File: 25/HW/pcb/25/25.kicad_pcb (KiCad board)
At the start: 2 copper layers, 31.5 x 31.5 mm, 5 parts

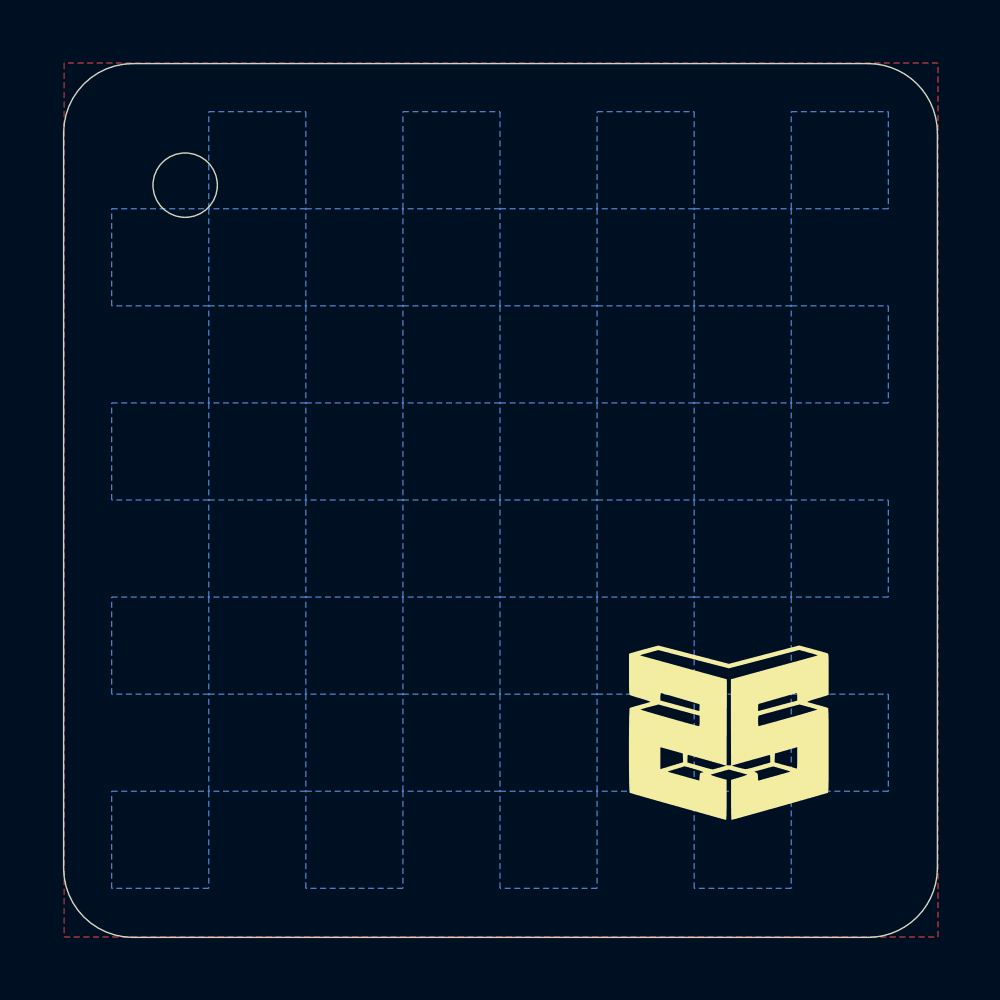
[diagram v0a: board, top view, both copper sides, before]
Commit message: Updated HW/ART and HW/PCB files for second batch of PCBs. First one had troubles with QR detection due to finder pattern with hole in it. Now only silkscreen on top, hole outside QR area (logo), and bigger drawings with metals on bottom
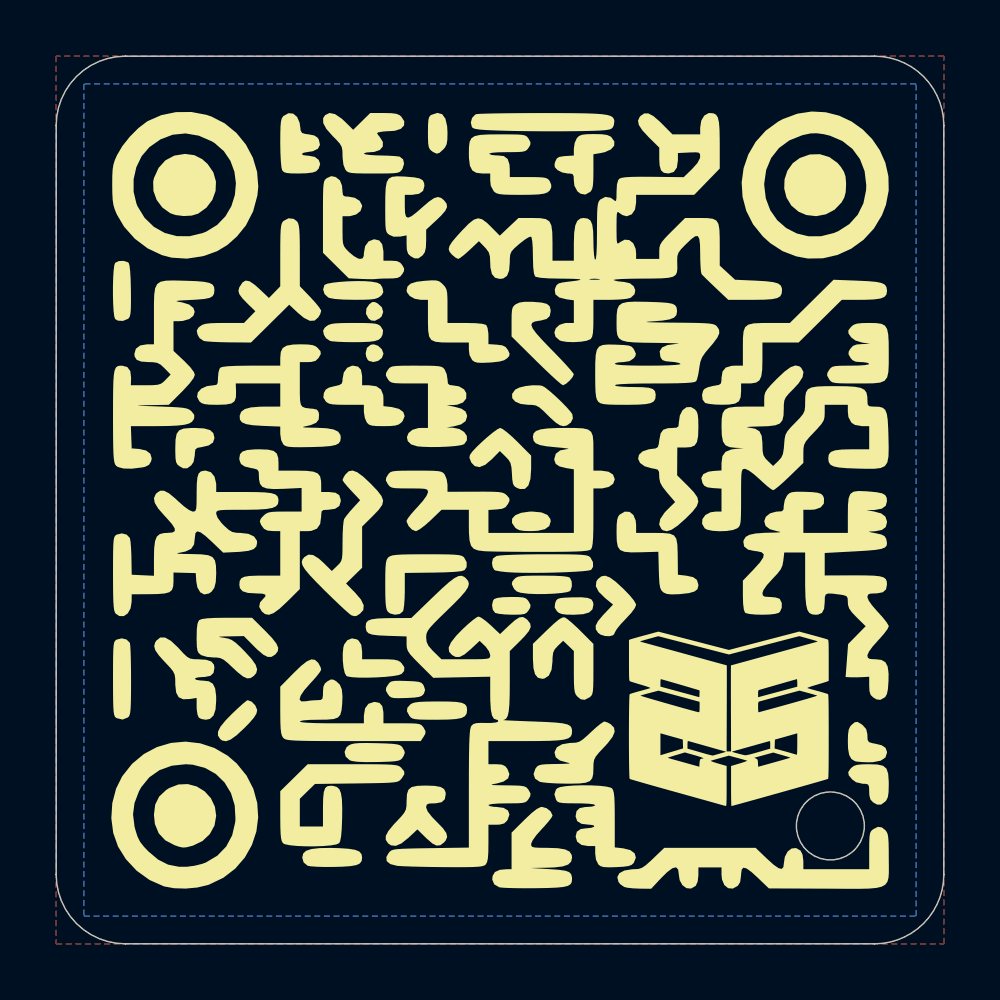
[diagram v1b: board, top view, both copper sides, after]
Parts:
- removed the G*** at (124.2, 53.2)
- removed the G*** at (127.8, 60.2)
- removed the G*** at (120.8, 56.8)
- added G***: LOGO, LOGO, B.Cu at (126.0, 62.0)
- added G***: LOGO, LOGO, B.Cu at (119.0, 55.0)
- added G***: LOGO, LOGO, B.Cu at (104.5, 69.0)
- moved G*** 0.50 mm to (123.8, 73.5)
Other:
- board size 31.5 x 31.5 mm -> 32 x 32 mm
- board text added: "The game ends when the King falls not when a pawn takes your Queen."
- board text removed: "The game ends when the King falls, not when a pawn takes your Queen."
